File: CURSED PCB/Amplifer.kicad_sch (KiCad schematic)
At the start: 12 parts, among them U6 OPA323, U7 MCP3562-E_ST

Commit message: Fixes to pranav sugestions
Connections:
- net +5V: no longer R8.1
- net GND: now also R8.2
- net at C14.1, R7.2, U6.3 (+): now also R8.1; no longer R8.2
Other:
- moved on the sheet: C14, R7, R8

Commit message: fix with ash
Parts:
- C15: value 1uF -> 100nF
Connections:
- net +5V: now also R7.2; no longer C14.2, R7.1
- net GND: now also C14.1, D4.1 (K), D4.3 (Cathode_2); no longer D4.2 (A)
- net at C15.1, R9.1, U6.4 (-): now also D4.2 (A); no longer D4.1 (K), D4.3 (Cathode_2)
- net at R8.1, U6.3 (+): now also C14.2, R7.1; no longer C14.1, R7.2
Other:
- moved on the sheet: C14, D4, R7, R8

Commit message: component fixes
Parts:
- C14: value 1u -> 0.1u
- C15: value 100nF -> 3245nF
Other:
- note added: "Math is done on a google sheets labbeled "Experimental & PCB Data Setup Master" under Transimpedance Amplifer"
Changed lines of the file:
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@@
 	(generator_version "9.0")
 	(paper "A4")
+	(text "Math is done on a google sheets labbeled \"Experimental & PCB Data Setup Master\" under Transimpedance Amplifer\n"
+		(exclude_from_sim no)
+		(at 146.304 130.556 0)
+		(effects
+			(font
+				(size 1.27 1.27)
+			)
+		)
+	)
 	(junction
 		(at 134.62 107.95)
@@
 			)
 		)
-		(property "Value" "100nF"
+		(property "Value" "3245nF"
 			(at 154.9463 120.65 90)
 			(effects
@@
 			)
 		)
-		(property "Value" "1u"
+		(property "Value" "0.1u"
 			(at 127 76.1935 0)
 			(effects

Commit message: text for reviwers
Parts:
- C15: value 3245nF -> 3200nF
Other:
- note added: "Math is done on a google sheets labbeled "Experimental & PCB Data Setup Master" under Transimpedance Amplifer Google sheet is found under payload 2026 under data magnement"
- note removed: "Math is done on a google sheets labbeled "Experimental & PCB Data Setup Master" under Transimpedance Amplifer"
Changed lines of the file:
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@@
 	(generator_version "9.0")
 	(paper "A4")
-	(text "Math is done on a google sheets labbeled \"Experimental & PCB Data Setup Master\" under Transimpedance Amplifer\n"
+	(text "Math is done on a google sheets labbeled \"Experimental & PCB Data Setup Master\" under Transimpedance Amplifer\nGoogle sheet is found under payload 2026 under data magnement "
 		(exclude_from_sim no)
 		(at 146.304 130.556 0)
@@
 			)
 		)
-		(property "Value" "3245nF"
+		(property "Value" "3200nF"
 			(at 154.9463 120.65 90)
 			(effects

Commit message: schematic changes
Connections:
- no-connect marks 7 -> 4
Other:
- note added: "These values are subject to change in expected freq changes"
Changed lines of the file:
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@@
 	(generator_version "9.0")
 	(paper "A4")
+	(text "These values are subject to change in expected freq changes"
+		(exclude_from_sim no)
+		(at 103.632 108.712 0)
+		(effects
+			(font
+				(size 1.27 1.27)
+			)
+		)
+	)
 	(text "Math is done on a google sheets labbeled \"Experimental & PCB Data Setup Master\" under Transimpedance Amplifer\nGoogle sheet is found under payload 2026 under data magnement "
 		(exclude_from_sim no)
-		(at 146.304 130.556 0)
+		(at 144.78 136.398 0)
 		(effects
 			(font
@@
 	)
 	(no_connect
-		(at 229.87 90.17)
-	)
-	(no_connect
 		(at 229.87 97.79)
 	)
 	(no_connect
-		(at 229.87 92.71)
-	)
-	(no_connect
-		(at 229.87 87.63)
-	)
-	(no_connect

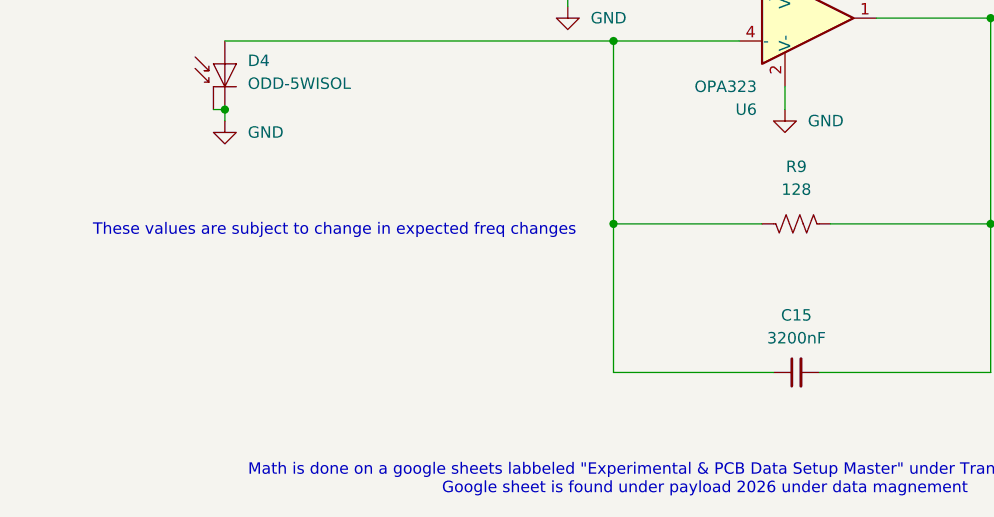
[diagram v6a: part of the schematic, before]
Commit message: footprint folde rupdate
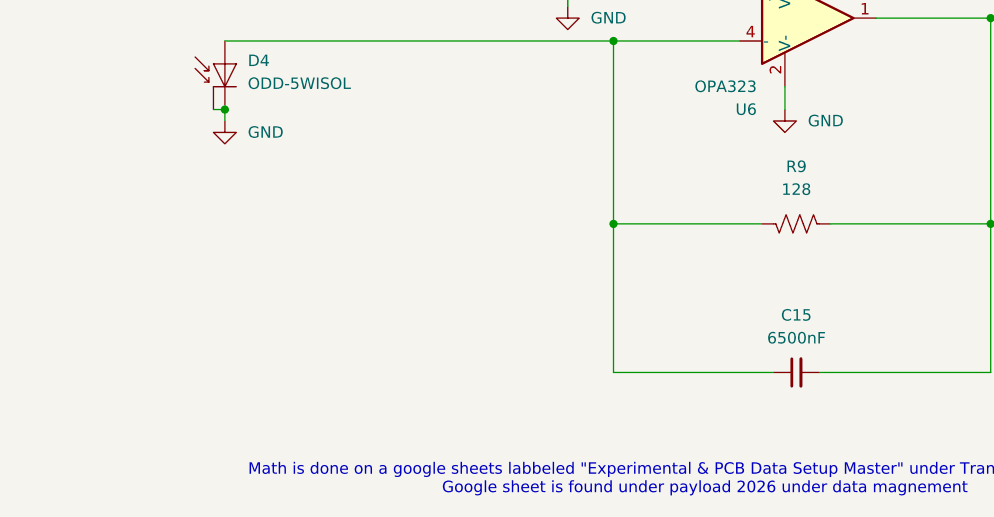
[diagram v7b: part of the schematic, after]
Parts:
- C15: value 3200nF -> 6500nF
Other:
- note removed: "These values are subject to change in expected freq changes"
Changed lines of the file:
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@@
 	(generator_version "9.0")
 	(paper "A4")
-	(text "These values are subject to change in expected freq changes"
-		(exclude_from_sim no)
-		(at 103.632 108.712 0)
-		(effects
-			(font
-				(size 1.27 1.27)
-			)
-		)
-	)
 	(text "Math is done on a google sheets labbeled \"Experimental & PCB Data Setup Master\" under Transimpedance Amplifer\nGoogle sheet is found under payload 2026 under data magnement "
 		(exclude_from_sim no)
@@
 			)
 		)
-		(property "Value" "3200nF"
+		(property "Value" "6500nF"
 			(at 154.9463 120.65 90)
 			(effects

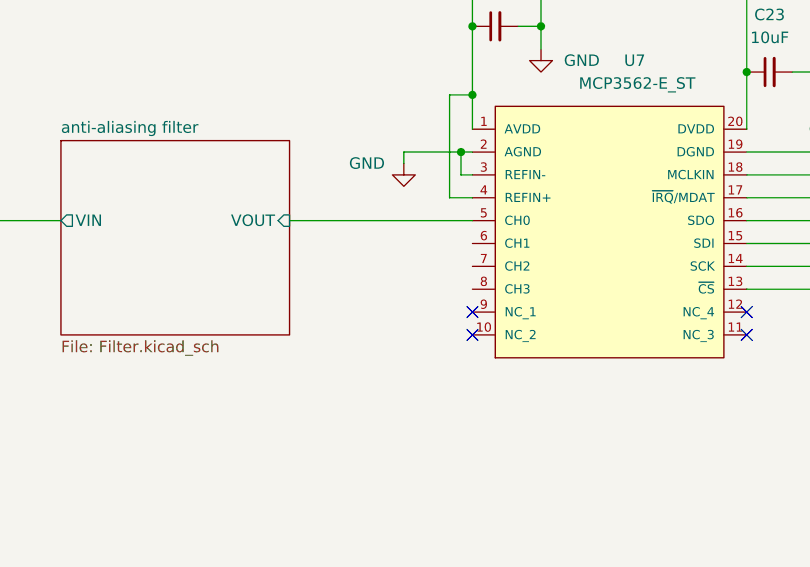
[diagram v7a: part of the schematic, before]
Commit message: updates traces and footprints
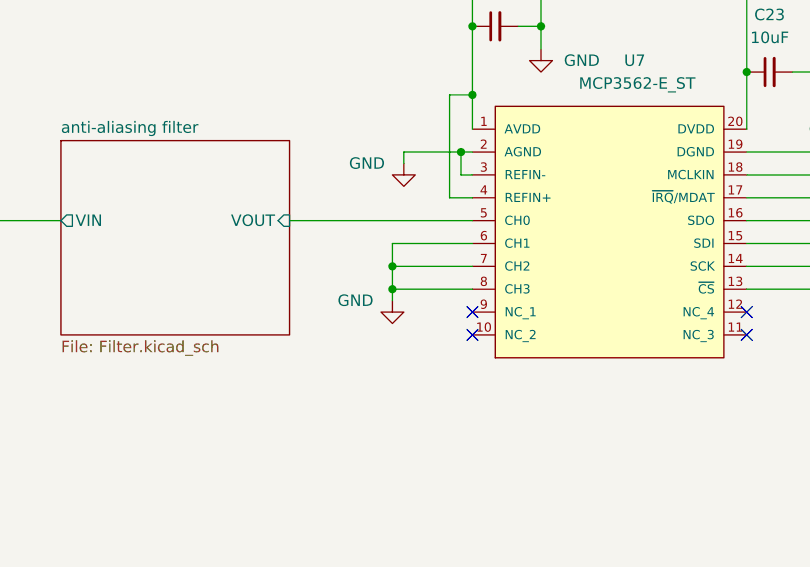
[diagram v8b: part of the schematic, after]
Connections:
- net GND: now also U7.6 (CH1), U7.7 (CH2), U7.8 (CH3)
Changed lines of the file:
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@@
+	)
+	(junction
+		(at 220.98 92.71)
+		(diameter 0)
+		(color 0 0 0 0)
 	)
 	(junction
@@
 	(junction
 		(at 228.6 77.47)
+		(diameter 0)
+		(color 0 0 0 0)
+	)
+	(junction
+		(at 220.98 90.17)
 		(diameter 0)
 		(color 0 0 0 0)
@@
 	(wire
 		(pts
+			(xy 220.98 87.63) (xy 220.98 90.17)
+		)
+		(stroke
+			(width 0)
+			(type default)
+		)
+	)
+	(wire
+		(pts
 			(xy 260.35 58.42) (xy 260.35 68.58)
 		)
@@
 	(wire
 		(pts
+			(xy 220.98 90.17) (xy 229.87 90.17)
+		)
+		(stroke
+			(width 0)
+			(type default)
+		)
+	)
+	(wire
+		(pts
 			(xy 237.49 66.04) (xy 237.49 63.5)
 		)
@@
 	(wire
 		(pts
+			(xy 220.98 90.17) (xy 220.98 92.71)
+		)
+		(stroke
+			(width 0)
+			(type default)
+		)
+	)
+	(wire
+		(pts
 			(xy 134.62 87.63) (xy 134.62 107.95)
 		)
@@
 	(wire
 		(pts
+			(xy 220.98 92.71) (xy 229.87 92.71)
+		)
+		(stroke
+			(width 0)
+			(type default)
+		)
+	)
+	(wire
+		(pts
 			(xy 176.53 85.09) (xy 176.53 107.95)
 		)
@@
 	(wire
 		(pts
+			(xy 220.98 92.71) (xy 220.98 93.98)
+		)
+		(stroke
+			(width 0)
+			(type default)
+		)
+	)
+	(wire
+		(pts
 			(xy 260.35 87.63) (xy 267.97 87.63)
+		)
+		(stroke
+			(width 0)
+			(type default)
+		)
+	)
+	(wire
+		(pts
+			(xy 229.87 87.63) (xy 220.98 87.63)
 		)
 		(stroke
@@
 					(unit 1)
 				)
+			)
+		)
+	)
+	(symbol
+		(lib_id "power:GND")
+		(at 220.98 93.98 0)
+		(unit 1)
+		(exclude_from_sim no)
+		(in_bom yes)
+		(on_board yes)
+		(dnp no)
+		(property "Reference" "#PWR056"
+			(at 220.98 100.33 0)
+			(effects
+				(font
+					(size 1.27 1.27)
+				)
+				(hide yes)
+			)
+		)
+		(property "Value" "GND"
+			(at 214.884 93.98 0)
+			(effects
+				(font
+					(size 1.27 1.27)
+				)
+				(justify left)
+			)
+		)
+		(property "Footprint" ""
+			(at 220.98 93.98 0)
+			(effects
+				(font
+					(size 1.27 1.27)
+				)
+				(hide yes)
+			)
+		)
+		(property "Datasheet" ""
+			(at 220.98 93.98 0)
+			(effects
+				(font
+					(size 1.27 1.27)
+				)
+				(hide yes)
+			)
+		)
+		(property "Description" "Power symbol creates a global label with name \"GND\" , ground"
+			(at 220.98 93.98 0)
+			(effects
+				(font
+					(size 1.27 1.27)
+				)
+				(hide yes)
+			)
+		)
+		(pin "1"
+		)
+		(instances
+			(project "sensor_1"
+				(path "/9fb1a86f-679c-4b88-9ed1-932f4f414580/543706d6-8cb0-4c51-81f6-888765ec3907"
+					(reference "#PWR056")
+					(unit 1)
+				)
